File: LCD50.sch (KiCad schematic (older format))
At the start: 21 parts, among them Q10 IRLML2502, Q8 IRLML2502, Q9 IRLML2502, U20 xc7z020clg484

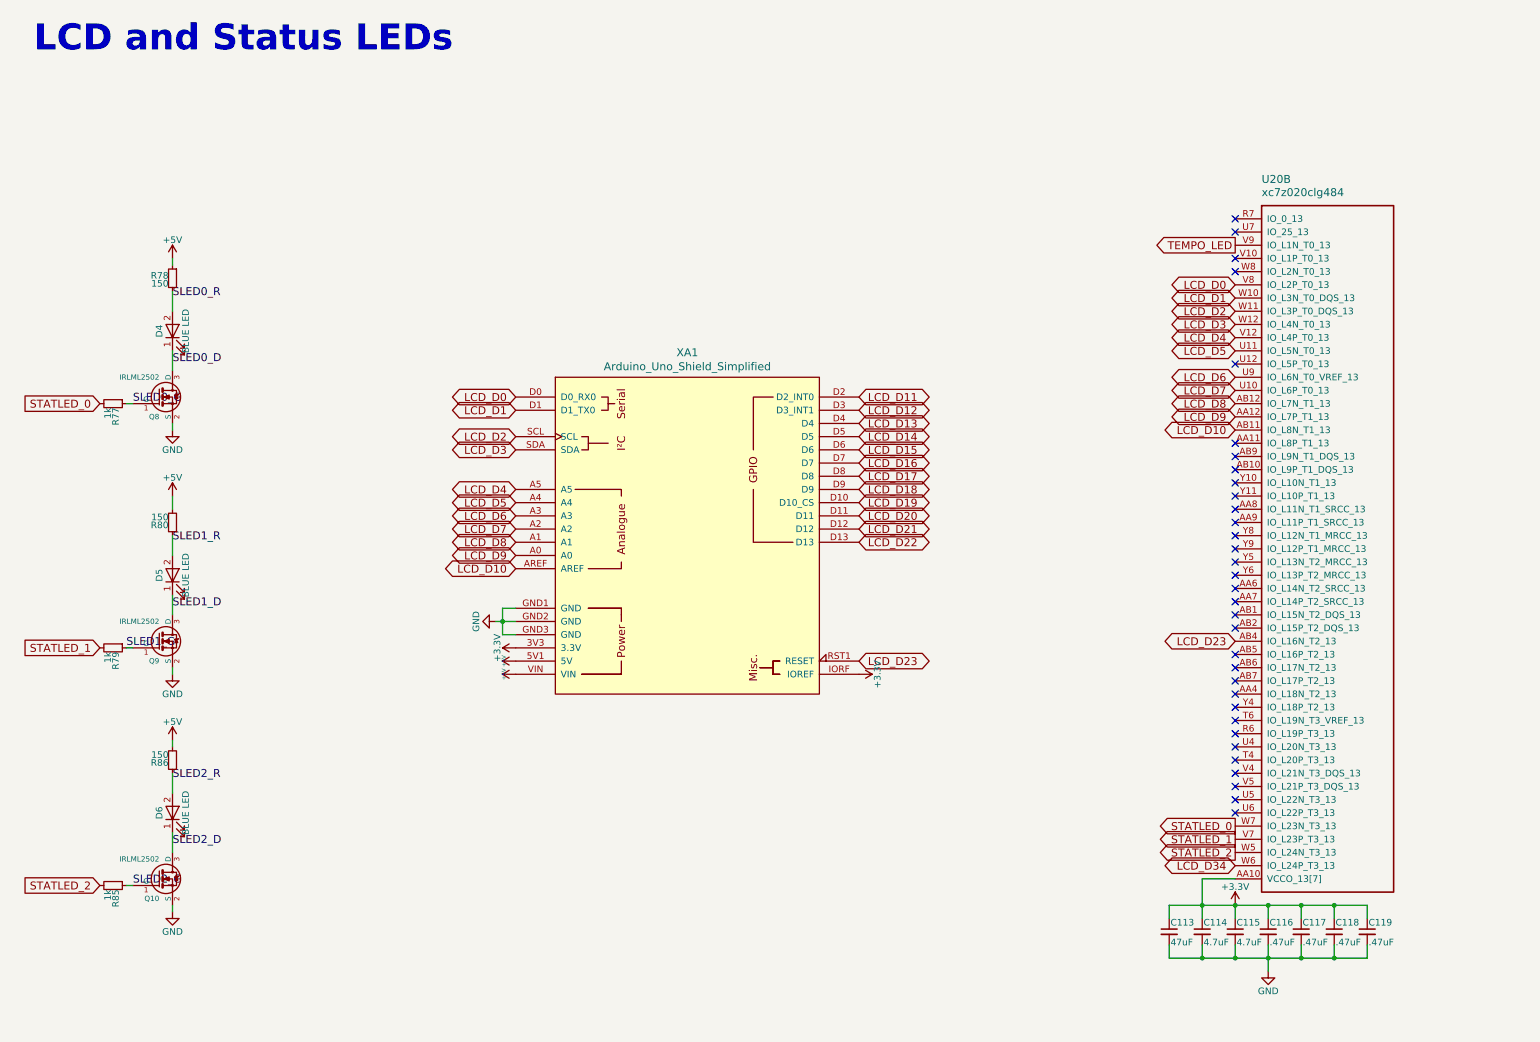
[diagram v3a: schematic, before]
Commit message: routed most of HDMI, I2S, and Arduino-type interfaces
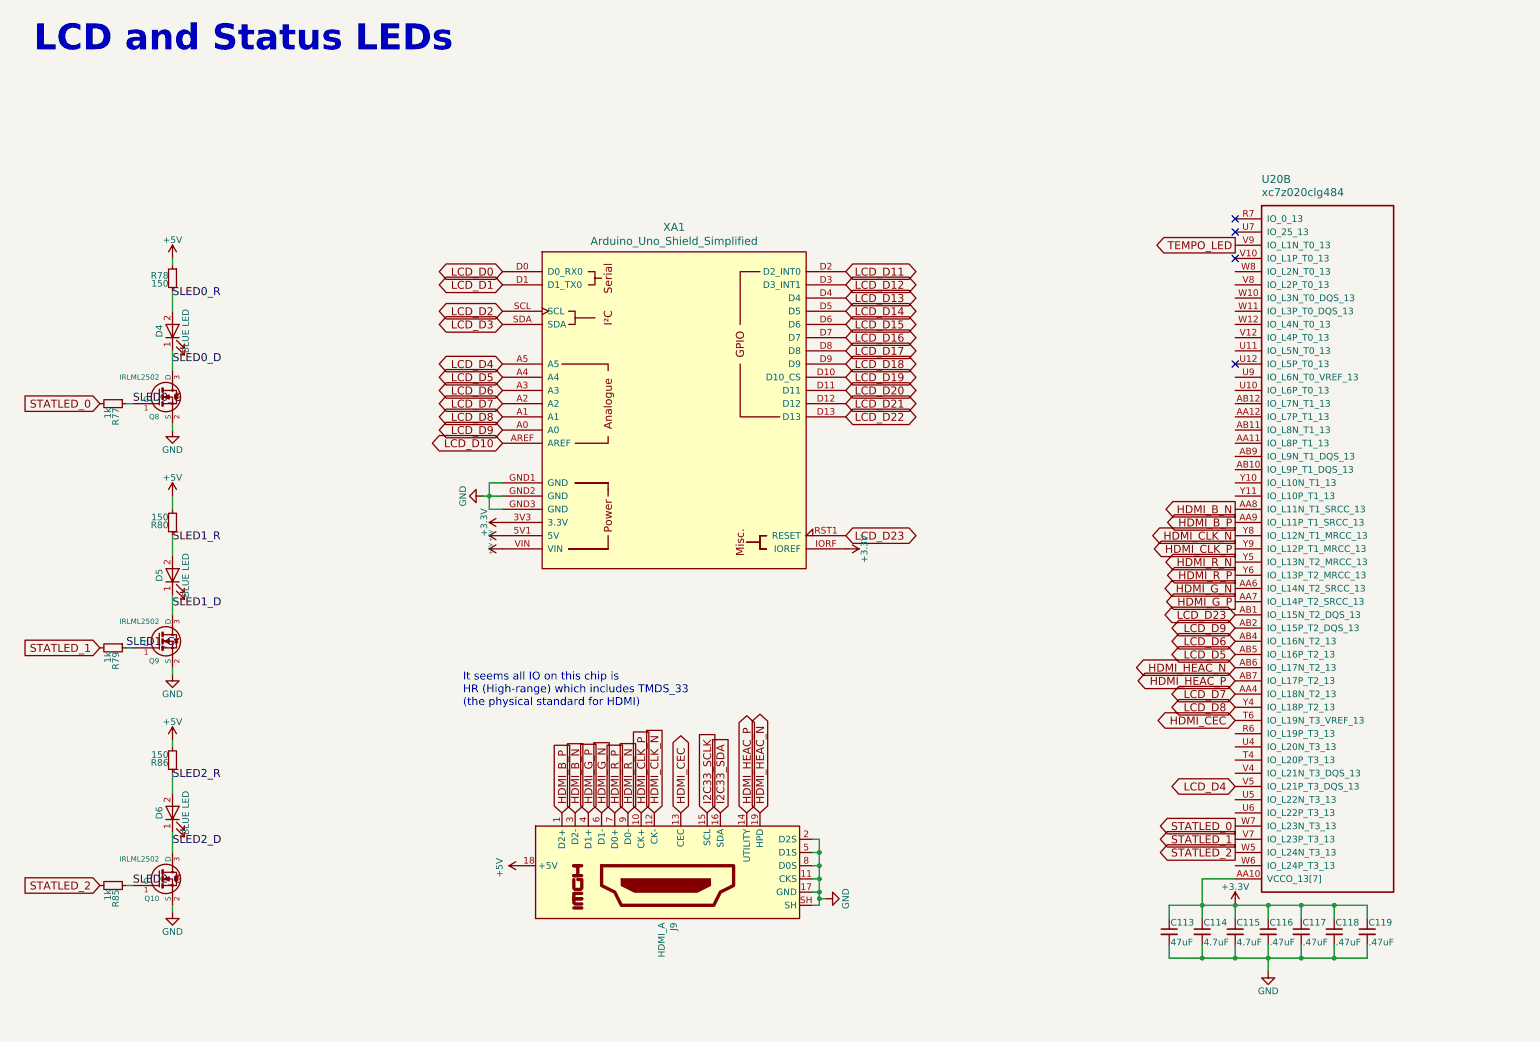
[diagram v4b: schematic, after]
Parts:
- added J9: HDMI_A, DFTcustom:10029449-111RLF, symbol Connector:HDMI_A
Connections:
- net +5V: now also J9.18 (+5V)
- net GND: now also J9.11 (CKS), J9.17 (GND), J9.2 (D2S), J9.5 (D1S), J9.8 (D0S), J9.SH
- net LCD_D0: no longer U20.V8 (IO_L2P_T0_13)
- net LCD_D1: no longer U20.W10 (IO_L3N_T0_DQS_13)
- net LCD_D10: no longer U20.AB11 (IO_L8N_T1_13)
- net LCD_D2: no longer U20.W11 (IO_L3P_T0_DQS_13)
- net LCD_D23: now also U20.AB1 (IO_L15N_T2_DQS_13); no longer U20.AB4 (IO_L16N_T2_13)
- net LCD_D3: no longer U20.W12 (IO_L4N_T0_13)
- net LCD_D4: now also U20.V5 (IO_L21P_T3_DQS_13); no longer U20.V12 (IO_L4P_T0_13)
- net LCD_D5: now also U20.AB5 (IO_L16P_T2_13); no longer U20.U11 (IO_L5N_T0_13)
- net LCD_D6: now also U20.AB4 (IO_L16N_T2_13); no longer U20.U9 (IO_L6N_T0_VREF_13)
- net LCD_D7: now also U20.AA4 (IO_L18N_T2_13); no longer U20.U10 (IO_L6P_T0_13)
- net LCD_D8: now also U20.Y4 (IO_L18P_T2_13); no longer U20.AB12 (IO_L7N_T1_13)
- net LCD_D9: now also U20.AB2 (IO_L15P_T2_DQS_13); no longer U20.AA12 (IO_L7P_T1_13)
- net HDMI_G_N: now reaches U20.AA6 (IO_L14N_T2_SRCC_13)
- net HDMI_G_N: now also J9.6 (D1-)
- net HDMI_G_P: now reaches U20.AA7 (IO_L14P_T2_SRCC_13)
- net HDMI_G_P: now also J9.4 (D1+)
- net HDMI_B_N: now reaches U20.AA8 (IO_L11N_T1_SRCC_13)
- net HDMI_B_N: now also J9.3 (D2-)
- net HDMI_B_P: now reaches U20.AA9 (IO_L11P_T1_SRCC_13)
- net HDMI_B_P: now also J9.1 (D2+)
- net HDMI_HEAC_N: now reaches U20.AB6 (IO_L17N_T2_13)
- net HDMI_HEAC_N: now also J9.19 (HPD)
- net HDMI_HEAC_P: now reaches U20.AB7 (IO_L17P_T2_13)
- net HDMI_HEAC_P: now also J9.14 (UTILITY)
- net HDMI_CEC: now reaches U20.T6 (IO_L19N_T3_VREF_13)
- net HDMI_CEC: now also J9.13 (CEC)
- net HDMI_R_N: now reaches U20.Y5 (IO_L13N_T2_MRCC_13)
- net HDMI_R_N: now also J9.9 (D0-)
- net HDMI_R_P: now reaches U20.Y6 (IO_L13P_T2_MRCC_13)
- net HDMI_R_P: now also J9.7 (D0+)
- net HDMI_CLK_N: now reaches U20.Y8 (IO_L12N_T1_MRCC_13)
- net HDMI_CLK_N: now also J9.12 (CK-)
- net HDMI_CLK_P: now reaches U20.Y9 (IO_L12P_T1_MRCC_13)
- net HDMI_CLK_P: now also J9.10 (CK+)
- net LCD_D34: no longer names the net of U20.W6 (IO_L24P_T3_13)
- new net I2C33_SCLK: J9.15 (SCL)
- new net I2C33_SDA: J9.16 (SDA)
- no-connect marks 33 -> 4
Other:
- note added: "It seems all IO on this chip is \nHR (High-range) which includes TMDS_33\n(the physical standard for HDMI)"
- moved on the sheet: XA1

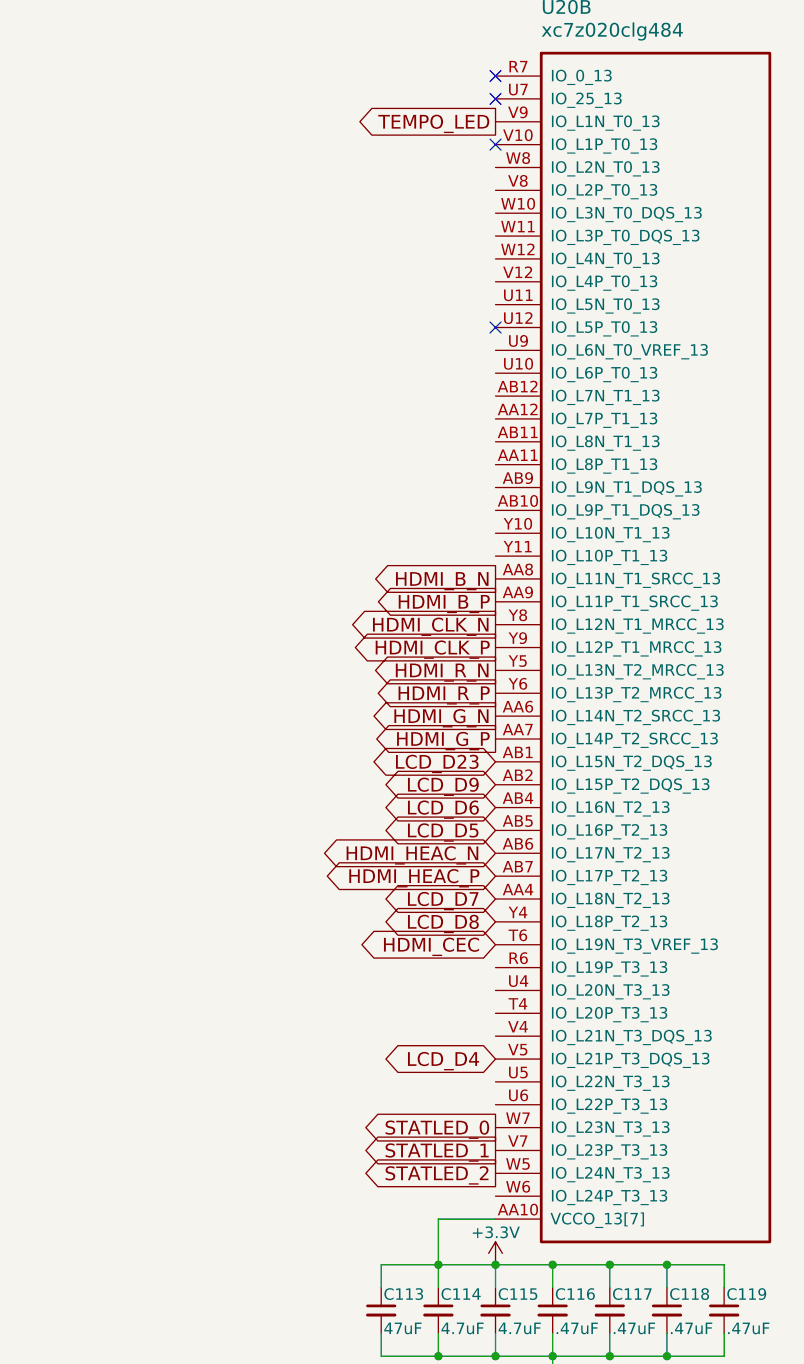
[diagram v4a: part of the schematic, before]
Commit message: routed a few things, about to remove power jack and 5V regulator
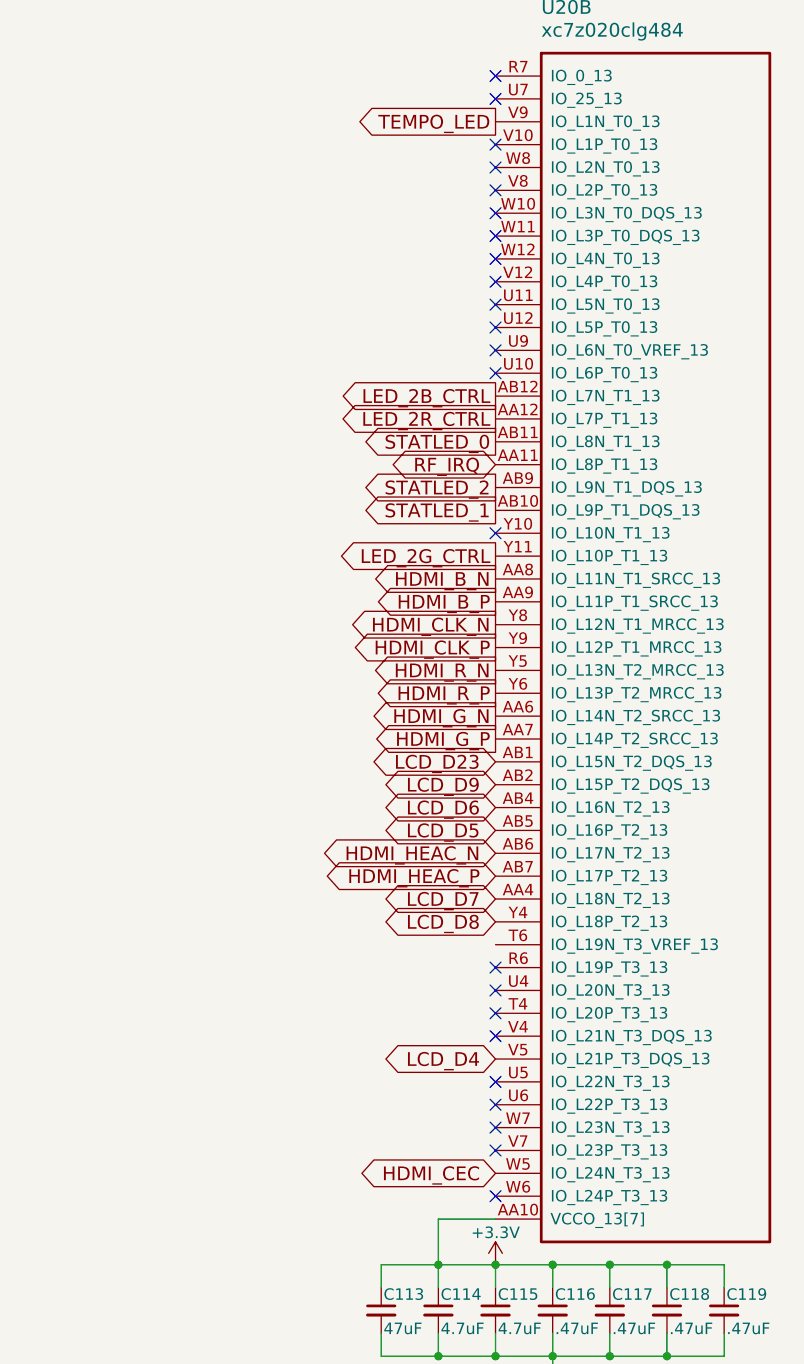
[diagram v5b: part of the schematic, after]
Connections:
- net HDMI_CEC: now also U20.W5 (IO_L24N_T3_13); no longer U20.T6 (IO_L19N_T3_VREF_13)
- net STATLED_0: now also U20.AB11 (IO_L8N_T1_13); no longer U20.W7 (IO_L23N_T3_13)
- net STATLED_1: now also U20.AB10 (IO_L9P_T1_DQS_13); no longer U20.V7 (IO_L23P_T3_13)
- net STATLED_2: now also U20.AB9 (IO_L9N_T1_DQS_13); no longer U20.W5 (IO_L24N_T3_13)
- net RF_IRQ: now reaches U20.AA11 (IO_L8P_T1_13)
- net LED_2R_CTRL: now reaches U20.AA12 (IO_L7P_T1_13)
- net LED_2B_CTRL: now reaches U20.AB12 (IO_L7N_T1_13)
- net LED_2G_CTRL: now reaches U20.Y11 (IO_L10P_T1_13)
- no-connect marks 4 -> 23
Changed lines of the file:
@@
 Wire Wire Line
 	1300 2800 1300 2950
-Text GLabel 9350 6400 0    60   Output ~ 0
+Text GLabel 9350 3400 0    60   Output ~ 0
 STATLED_0
-Text GLabel 9350 6500 0    60   Output ~ 0
+Text GLabel 9350 3700 0    60   Output ~ 0
 STATLED_1
-Text GLabel 9350 6600 0    60   Output ~ 0
+Text GLabel 9350 3600 0    60   Output ~ 0
 STATLED_2
 NoConn ~ 9350 2100
 Text Notes 250  550  0    197  ~ 39
 LCD and Status LEDs
-$Comp
-L xilinx7:xc7z020clg484 U20
-U 2 1 5CD35FBB
-P 9350 1800
-F 0 "U20" H 9550 2100 60  0000 L CNN
-F 1 "xc7z020clg484" H 9550 2000 60  0000 L CNN
-F 2 "DFTcustom:BGA-484_19.0x19.0mm_Layout22x22_P0.80mm_dia0.40mm" H 9350 1800 60  0001 C CNN
-F 3 "" H 9350 1800 60  0001 C CNN
-	2    9350 1800
-	1    0    0    -1
-$EndComp
 $Comp
 L power:GND #PWR?
@@
 Text GLabel 9350 4500 0    60   Output ~ 0
 HDMI_R_P
-Text GLabel 9350 5600 0    60   BiDi ~ 0
+Text GLabel 9350 6600 0    60   BiDi ~ 0
 HDMI_CEC
 Text Notes 3500 5500 0    60   ~ 0
@@
 Text GLabel 9350 4300 0    60   Output ~ 0
 HDMI_CLK_P
+NoConn ~ 9350 2200
+NoConn ~ 9350 2300
+NoConn ~ 9350 2400
+NoConn ~ 9350 2500
+NoConn ~ 9350 2600
+NoConn ~ 9350 2700
+NoConn ~ 9350 2800
+NoConn ~ 9350 3000
+NoConn ~ 9350 3100
+NoConn ~ 9350 3800
+NoConn ~ 9350 5700
+NoConn ~ 9350 5800
+NoConn ~ 9350 5900
+NoConn ~ 9350 6000
+NoConn ~ 9350 6200
+NoConn ~ 9350 6300
+NoConn ~ 9350 6700
+$Comp
+L xilinx7:xc7z020clg484 U20
+U 2 1 5CD35FBB
+P 9350 1800
+F 0 "U20" H 9550 2100 60  0000 L CNN
+F 1 "xc7z020clg484" H 9550 2000 60  0000 L CNN
+F 2 "DFTcustom:BGA-484_19.0x19.0mm_Layout22x22_P0.80mm_dia0.40mm" H 9350 1800 60  0001 C CNN
+F 3 "" H 9350 1800 60  0001 C CNN
+	2    9350 1800
+	1    0    0    -1
+$EndComp
+Text GLabel 9350 3500 0    60   BiDi ~ 0
+RF_IRQ
+Text GLabel 9350 3200 0    60   Output ~ 0
+LED_2B_CTRL
+Text GLabel 9350 3900 0    60   Output ~ 0
+LED_2G_CTRL
+Text GLabel 9350 3300 0    60   Output ~ 0
+LED_2R_CTRL
+NoConn ~ 9350 6400
+NoConn ~ 9350 6500
 $EndSCHEMATC

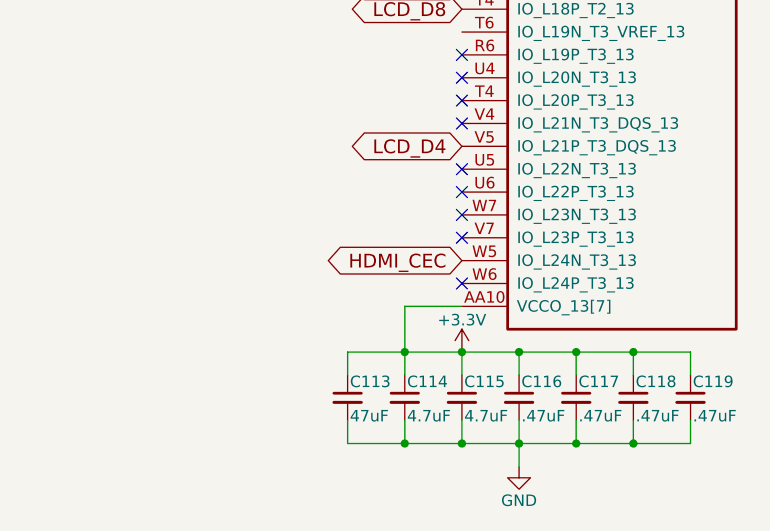
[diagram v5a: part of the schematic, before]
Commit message: downto 70 unrouted. moved SD interface back to MIO
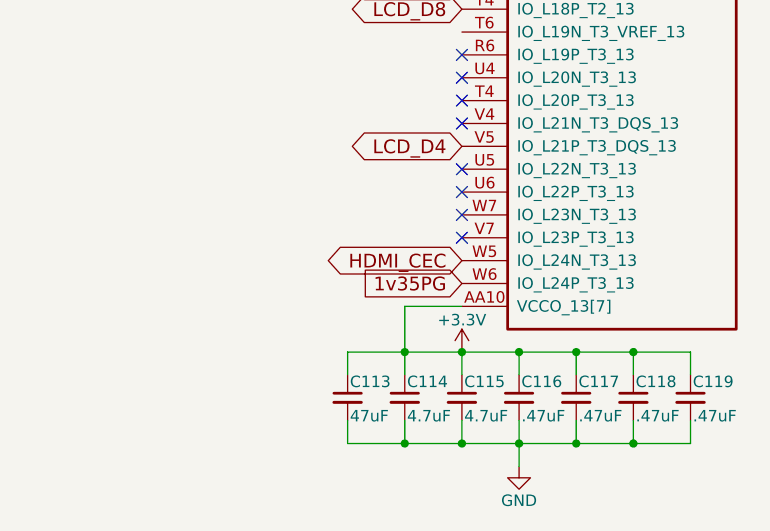
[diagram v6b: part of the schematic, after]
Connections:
- net 1v35PG: now reaches U20.W6 (IO_L24P_T3_13)
- no-connect marks 23 -> 22
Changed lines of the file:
@@
 NoConn ~ 9350 6200
 NoConn ~ 9350 6300
-NoConn ~ 9350 6700
 $Comp
 L xilinx7:xc7z020clg484 U20
@@
 NoConn ~ 9350 6400
 NoConn ~ 9350 6500
+Text GLabel 9350 6700 0    60   Input ~ 0
+1v35PG
 $EndSCHEMATC

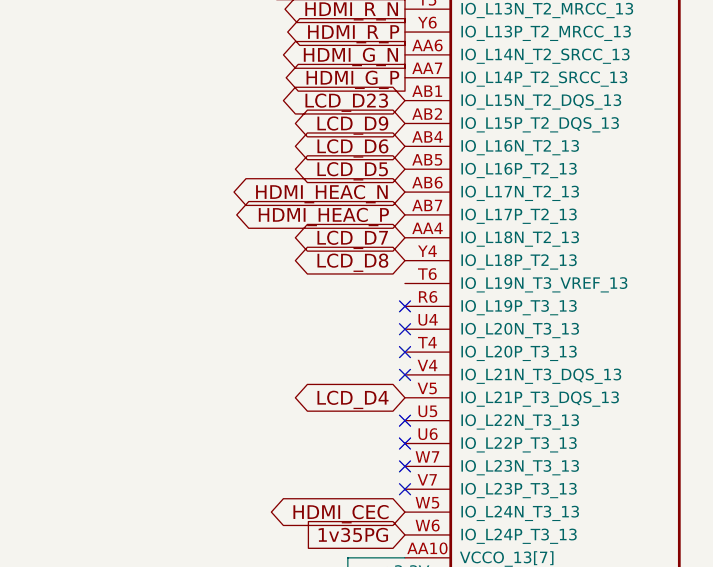
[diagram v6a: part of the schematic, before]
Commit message: DRC passes with only GNDTIE errors. no unconnected. power plane quality unknown
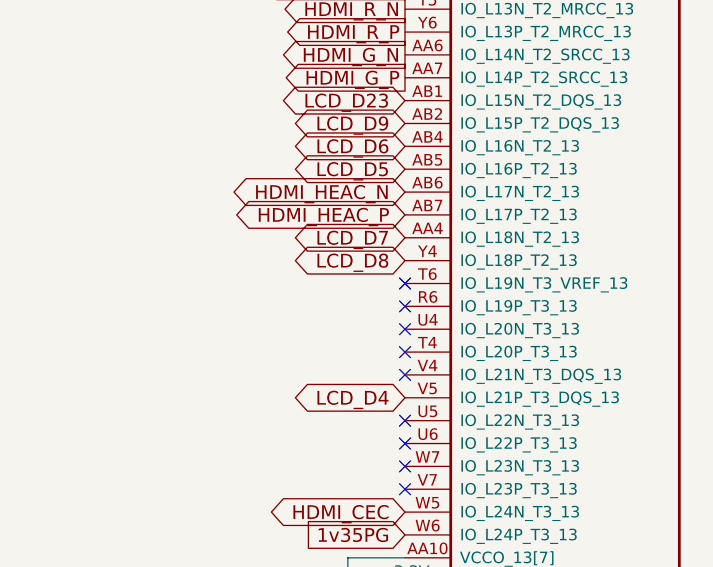
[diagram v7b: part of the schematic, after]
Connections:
- no-connect marks 22 -> 23
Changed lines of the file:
@@
 Text GLabel 9350 6700 0    60   Input ~ 0
 1v35PG
+NoConn ~ 9350 5600
 $EndSCHEMATC
